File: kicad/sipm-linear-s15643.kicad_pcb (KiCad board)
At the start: 4 copper layers, 92.2 x 68.9 mm, 164 parts, among them J1 SSQ-103-01-G-D, J12 Conn_Coaxial, J13 Conn_Coaxial, J2 Conn_Coaxial, J3 Conn_Coaxial, J4 Conn_Coaxial, J5 Conn_Coaxial, J6 Conn_Coaxial, J7 Conn_Coaxial, J8 Conn_Coaxial, J9 Conn_Coaxial, U1 OPA847IDBVT, U12 OPA847IDBVT, U13 OPA847IDBVT, U2 S15643, U3 OPA847IDBVT, U4 OPA847IDBVT, U5 OPA847IDBVT, U6 OPA847IDBVT, U7 OPA847IDBVT, U8 OPA847IDBVT, U9 OPA847IDBVT

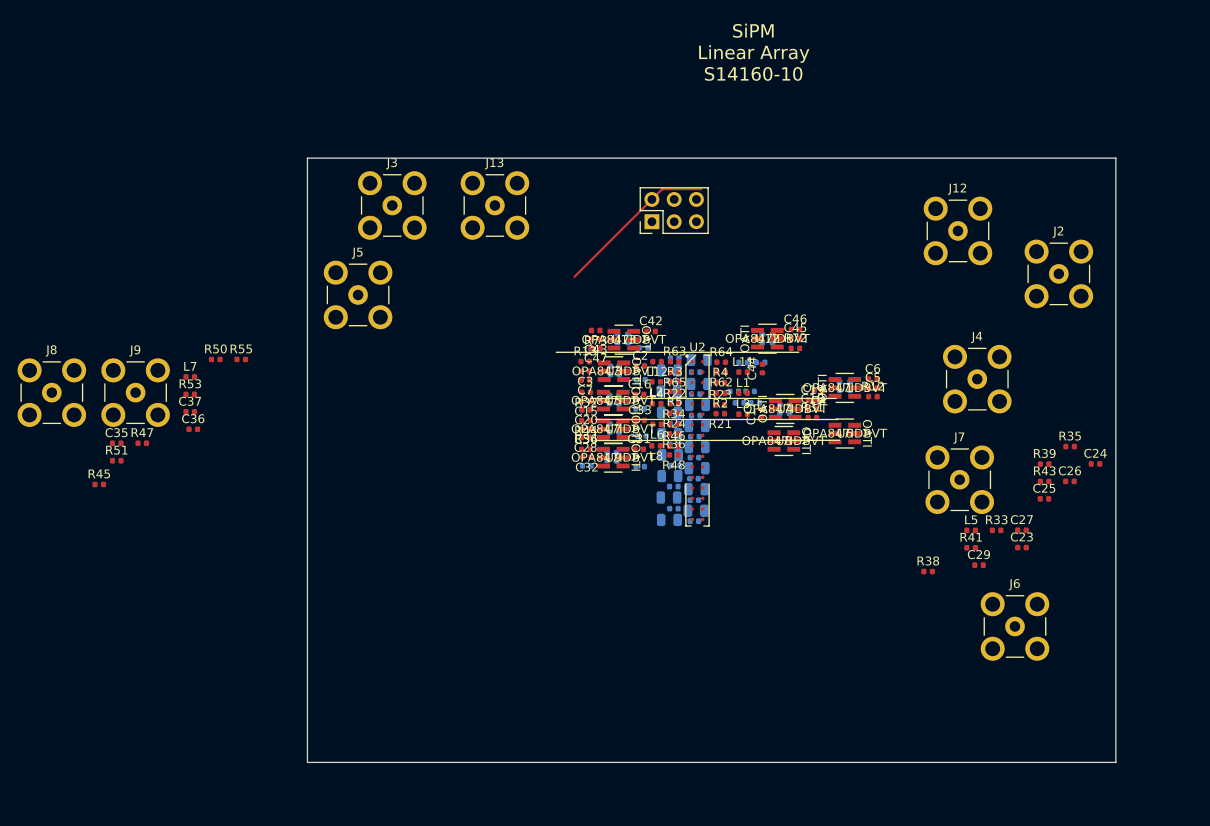
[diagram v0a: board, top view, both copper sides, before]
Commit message: Update layout for the new footprint
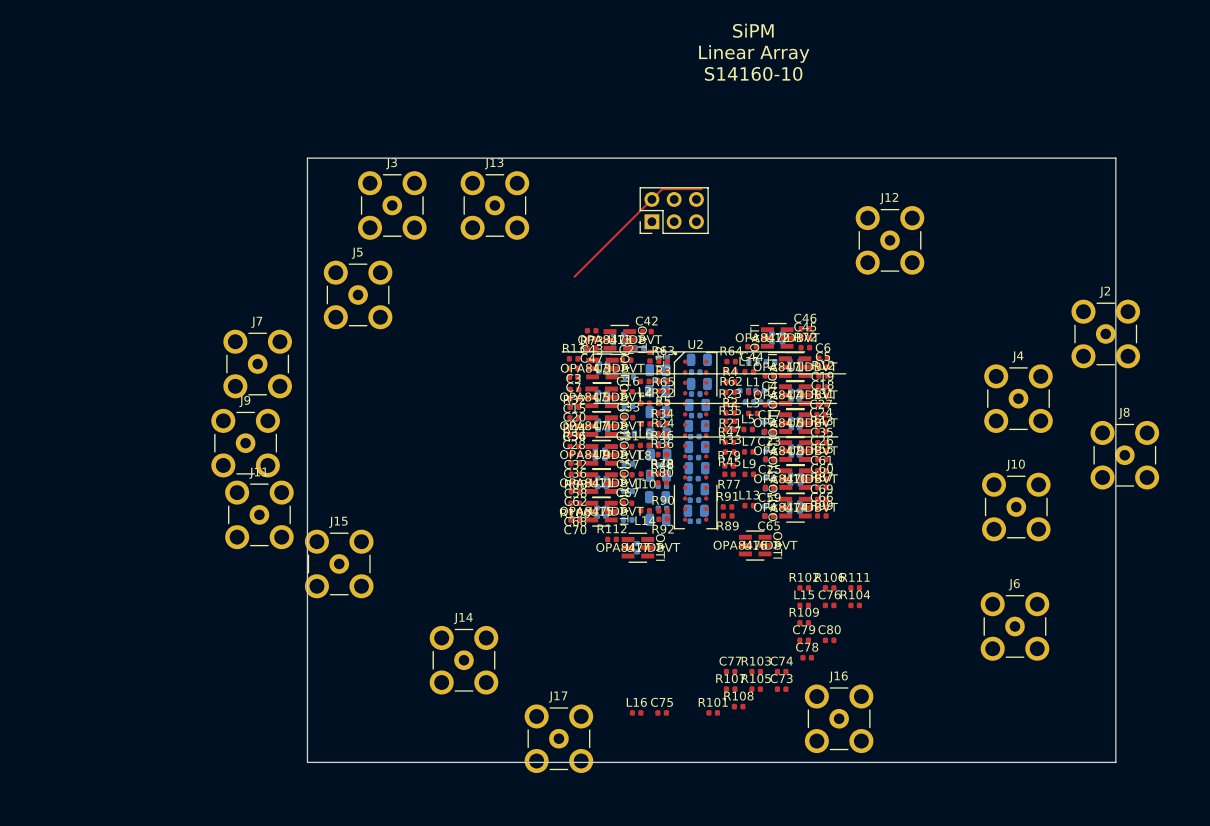
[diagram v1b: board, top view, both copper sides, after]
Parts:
- added C57: 1u, Capacitor_SMD:C_0402_1005Metric, F.Cu at (175.8, 105.3)
- added C58: 1u, Capacitor_SMD:C_0402_1005Metric, F.Cu at (169.9, 106.3)
- added C59: 1u, Capacitor_SMD:C_0402_1005Metric, F.Cu at (192.0, 106.8)
- added C60: 1u, Capacitor_SMD:C_0402_1005Metric, F.Cu at (198.0, 105.8)
- added C61: 1u, Capacitor_SMD:C_0402_1005Metric, F.Cu at (198.0, 104.8)
- added C62: 1u, Capacitor_SMD:C_0402_1005Metric, F.Cu at (169.9, 107.2)
- added C63: 1p, Capacitor_SMD:C_0402_1005Metric, B.Cu at (195.5, 105.9)
- added C64: 1p, Capacitor_SMD:C_0402_1005Metric, B.Cu at (173.4, 106.2)
- added C65: 1u, Capacitor_SMD:C_0402_1005Metric, F.Cu at (192.0, 110.0)
- added C66: 1u, Capacitor_SMD:C_0402_1005Metric, F.Cu at (198.0, 109.0)
- added C67: 1u, Capacitor_SMD:C_0402_1005Metric, F.Cu at (175.8, 108.5)
- added C68: 1u, Capacitor_SMD:C_0402_1005Metric, F.Cu at (169.9, 109.5)
- added C69: 1u, Capacitor_SMD:C_0402_1005Metric, F.Cu at (198.0, 108.1)
- added C70: 1u, Capacitor_SMD:C_0402_1005Metric, F.Cu at (169.9, 110.5)
- added C71: 1p, Capacitor_SMD:C_0402_1005Metric, B.Cu at (194.3, 109.0)
- added C72: 1p, Capacitor_SMD:C_0402_1005Metric, B.Cu at (173.4, 109.6)
- added C73: 1u, Capacitor_SMD:C_0402_1005Metric, F.Cu at (193.4, 129.8)
- added C74: 1u, Capacitor_SMD:C_0402_1005Metric, F.Cu at (193.4, 127.8)
- added C75: 1u, Capacitor_SMD:C_0402_1005Metric, F.Cu at (179.8, 132.5)
- added C76: 1u, Capacitor_SMD:C_0402_1005Metric, F.Cu at (198.9, 120.2)
- added C77: 1u, Capacitor_SMD:C_0402_1005Metric, F.Cu at (187.6, 127.8)
- added C78: 1u, Capacitor_SMD:C_0402_1005Metric, F.Cu at (196.3, 126.2)
- added C79: 1p, Capacitor_SMD:C_0402_1005Metric, F.Cu at (196.0, 124.2)
- added C80: 1p, Capacitor_SMD:C_0402_1005Metric, F.Cu at (198.9, 124.2)
- added J10: Conn_Coaxial, Connector_Coaxial:SMB_Jack_Vertical, F.Cu at (220.2, 109.0)
- added J11: Conn_Coaxial, Connector_Coaxial:SMB_Jack_Vertical, F.Cu at (133.8, 109.9)
- added J14: Conn_Coaxial, Connector_Coaxial:SMB_Jack_Vertical, F.Cu at (157.2, 126.5)
- added J15: Conn_Coaxial, Connector_Coaxial:SMB_Jack_Vertical, F.Cu at (142.9, 115.5)
- added J16: Conn_Coaxial, Connector_Coaxial:SMB_Jack_Vertical, F.Cu at (199.9, 133.1)
- added J17: Conn_Coaxial, Connector_Coaxial:SMB_Jack_Vertical, F.Cu at (168.0, 135.4)
- added L10: 0.033uH, footprints:C_0402_1005Metric, F.Cu at (177.9, 105.2)
- added L13: 0.033uH, footprints:C_0402_1005Metric, F.Cu at (189.7, 108.8)
- added L14: 0.033uH, footprints:C_0402_1005Metric, F.Cu at (177.8, 109.4)
- added L15: 0.033uH, footprints:C_0402_1005Metric, F.Cu at (196.0, 120.2)
- added L16: 0.033uH, footprints:C_0402_1005Metric, F.Cu at (176.9, 132.5)
- added L9: 0.033uH, footprints:C_0402_1005Metric, F.Cu at (189.7, 105.2)
- added R100: 50, footprints:R_0402_1005Metric, F.Cu at (169.8, 108.5)
- added R101: 3.3, footprints:R_0402_1005Metric, F.Cu at (185.6, 132.5)
- added R102: 3.3, footprints:R_0402_1005Metric, F.Cu at (196.0, 118.2)
- added R103: 33, footprints:R_0402_1005Metric, F.Cu at (190.5, 127.8)
- added R104: 33, footprints:R_0402_1005Metric, F.Cu at (201.8, 120.2)
- added R105: 5000, footprints:R_0402_1005Metric, F.Cu at (190.5, 129.8)
- added R106: 5000, footprints:R_0402_1005Metric, F.Cu at (198.9, 118.2)
- added R107: 5000, footprints:R_0402_1005Metric, F.Cu at (187.6, 129.8)
- added R108: 5000, footprints:R_0402_1005Metric, F.Cu at (188.5, 131.7)
- added R109: 1.5k, footprints:R_0402_1005Metric, F.Cu at (196.0, 122.2)
- added R110: 1.5k, footprints:R_0402_1005Metric, B.Cu at (176.9, 113.6)
- added R111: 50, footprints:R_0402_1005Metric, F.Cu at (201.8, 118.2)
- added R112: 50, footprints:R_0402_1005Metric, F.Cu at (174.1, 112.7)
- added R77: 3.3, footprints:R_0402_1005Metric, F.Cu at (187.4, 105.2)
- added R78: 3.3, footprints:R_0402_1005Metric, F.Cu at (179.8, 105.2)
- added R79: 33, footprints:R_0402_1005Metric, F.Cu at (187.4, 104.3)
- added R80: 33, footprints:R_0402_1005Metric, F.Cu at (179.8, 106.2)
- added R81: 5000, footprints:R_0402_1005Metric, B.Cu at (175.9, 107.2)
- added R82: 5000, footprints:R_0402_1005Metric, B.Cu at (192.0, 105.7)
- added R83: 5000, footprints:R_0402_1005Metric, B.Cu at (192.0, 106.9)
- added R84: 5000, footprints:R_0402_1005Metric, B.Cu at (169.9, 107.2)
- added R85: 1.5k, footprints:R_0402_1005Metric, B.Cu at (194.4, 105.8)
- added R86: 1.5k, footprints:R_0402_1005Metric, B.Cu at (172.4, 106.2)
- added R87: 50, footprints:R_0402_1005Metric, F.Cu at (198.0, 106.8)
- added R88: 50, footprints:R_0402_1005Metric, F.Cu at (169.9, 105.3)
- added R89: 3.3, footprints:R_0402_1005Metric, F.Cu at (187.2, 110.0)
- added R90: 3.3, footprints:R_0402_1005Metric, F.Cu at (179.9, 109.4)
- added R91: 33, footprints:R_0402_1005Metric, F.Cu at (187.2, 109.0)
- added R92: 33, footprints:R_0402_1005Metric, F.Cu at (179.9, 110.4)
- added R93: 5000, footprints:R_0402_1005Metric, B.Cu at (175.8, 110.5)
- added R94: 5000, footprints:R_0402_1005Metric, B.Cu at (192.0, 110.0)
- added R95: 5000, footprints:R_0402_1005Metric, B.Cu at (192.0, 109.0)
- added R96: 5000, footprints:R_0402_1005Metric, B.Cu at (169.9, 110.5)
- added R97: 1.5k, footprints:R_0402_1005Metric, B.Cu at (195.5, 109.0)
- added R98: 1.5k, footprints:R_0402_1005Metric, B.Cu at (172.3, 109.6)
- added R99: 50, footprints:R_0402_1005Metric, F.Cu at (198.0, 110.0)
- added U10: OPA847IDBVT, footprints:OPA847IDBVT, F.Cu at (195.0, 105.8)
- added U11: OPA847IDBVT, footprints:OPA847IDBVT, F.Cu at (172.9, 106.3)
- added U14: OPA847IDBVT, footprints:OPA847IDBVT, F.Cu at (195.0, 109.0)
- added U15: OPA847IDBVT, footprints:OPA847IDBVT, F.Cu at (172.8, 109.5)
- added U16: OPA847IDBVT, footprints:OPA847IDBVT, F.Cu at (190.4, 113.4)
- added U17: OPA847IDBVT, footprints:OPA847IDBVT, F.Cu at (177.0, 113.6)
- C29, C37, R38, R39, R41, R50, R51, R53: moved to B.Cu
- U2: footprint footprints:S15643-N16 -> S13615-1025:AF210729-S14160-x16
- moved J8 122.6 mm to (232.5, 103.1)
- moved J7 81.1 mm to (133.7, 92.7)
- moved C35 80.4 mm to (198.0, 101.7)
- moved R51 74.5 mm to (192.0, 103.5)
- moved R45 72.0 mm to (187.5, 102.7), turned to 180 degrees
- moved C37 69.6 mm to (195.4, 102.6), turned to -90 degrees
- moved R53 68.8 mm to (194.5, 102.6), turned to -90 degrees
- moved R55 67.2 mm to (198.0, 103.5)
- moved R47 67.0 mm to (187.4, 101.6)
- moved L7 64.3 mm to (189.7, 102.7)
- moved R50 64.0 mm to (192.1, 102.6), turned to 180 degrees
- moved C36 43.7 mm to (169.8, 104.0), turned to 180 degrees
- moved R35 38.9 mm to (187.5, 99.2)
- moved R33 32.5 mm to (187.5, 100.2), turned to 180 degrees
- moved C23 31.7 mm to (192.0, 100.4), turned to 180 degrees
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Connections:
- C50 pad 1: Net-(U2-Pad19) -> Net-(C50-Pad1)
- C51 pad 1: Net-(U2-Pad21) -> Net-(C51-Pad1)
- C52 pad 1: Net-(U2-Pad23) -> Net-(C52-Pad1)
- C53 pad 1: Net-(U2-Pad25) -> Net-(C53-Pad1)
- C54 pad 1: Net-(U2-Pad27) -> Net-(C54-Pad1)
- C55 pad 1: Net-(U2-Pad29) -> Net-(C55-Pad1)
- C56 pad 1: Net-(U2-Pad31) -> Net-(C56-Pad1)
- R60 pad 2: Net-(U2-Pad19) -> Net-(C50-Pad1)
- R61 pad 2: Net-(U2-Pad21) -> Net-(C51-Pad1)
- R66 pad 2: Net-(U2-Pad23) -> Net-(C52-Pad1)
- R67 pad 2: Net-(U2-Pad25) -> Net-(C53-Pad1)
- R74 pad 2: Net-(U2-Pad27) -> Net-(C54-Pad1)
- R75 pad 2: Net-(U2-Pad29) -> Net-(C55-Pad1)
- R76 pad 2: Net-(U2-Pad31) -> Net-(C56-Pad1)

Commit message: Update layout and fix array footprint
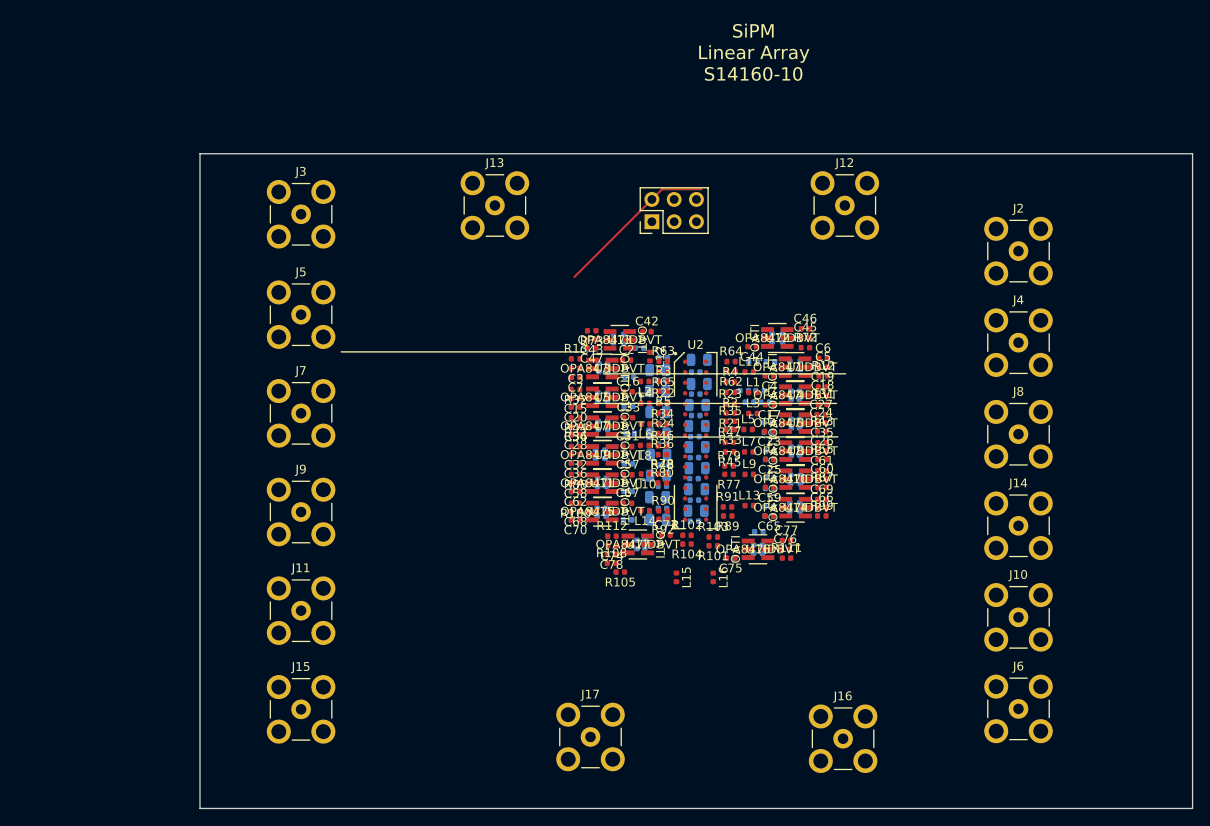
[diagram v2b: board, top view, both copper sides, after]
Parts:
- C79, C80, R106, R107, R109: moved to B.Cu
- J10, J11, J12, J13, J14, J15, J16, J17, J2, J3, J4, J5, J6, J7, J8, J9: footprint Connector_Coaxial:SMB_Jack_Vertical -> footprints:SMB_Jack_Vertical
- moved J14 65.1 mm to (220.4, 111.1)
- moved C78 25.2 mm to (174.0, 114.4), turned to 180 degrees
- moved C74 24.1 mm to (174.1, 113.4), turned to 180 degrees
- moved C80 23.8 mm to (177.8, 113.2), turned to -90 degrees
- moved C73 22.0 mm to (180.2, 112.2)
- moved R108 21.8 mm to (174.0, 115.4)
- moved R105 20.4 mm to (175.0, 116.4), turned to 180 degrees
- moved R104 20.4 mm to (182.6, 113.2), turned to 180 degrees
- moved C75 19.3 mm to (187.6, 114.8), turned to 180 degrees
- moved R101 19.1 mm to (185.6, 113.4), turned to 180 degrees
- moved R107 18.2 mm to (190.8, 111.8), turned to 180 degrees
- moved L16 17.8 mm to (185.6, 117.0), turned to -90 degrees
- moved J15 17.1 mm to (138.6, 132.1)
- moved C77 16.3 mm to (193.9, 112.8)
- moved R103 16.1 mm to (185.6, 112.4)
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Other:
- board size 92.2 x 68.9 mm -> 113.2 x 74.6 mm

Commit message: Update foot print for the revised hamamatsu part
They only have 2 cathode connections.  In addition, add a second power connector, since at least two power supplies are going to be needed.
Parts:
- removed C13, C50, C51, C52, C53, C54, C55, C56: 1u, Capacitor_SMD:C_0805_2012Metric
- removed R16, R17, R18, R19, R20, R57, R58, R60, R61, R66, R67, R74, R75, R76: 10, footprints:R_0402_1005Metric
- moved C12 8.93 mm to (184.0, 88.2), turned to 0 degrees
- moved C10 5.67 mm to (184.0, 90.2), turned to 0 degrees
- moved C11 0.75 mm to (184.0, 94.2), turned to 0 degrees
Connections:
- C1 pad 1: Net-(C1-Pad1) -> Net-(C11-Pad1)
- C10 pad 1: Net-(C10-Pad1) -> Net-(C11-Pad1)
- C12 pad 1: Net-(C12-Pad1) -> Net-(C11-Pad1)
- C39 pad 1: Net-(C39-Pad1) -> Net-(C14-Pad1)
- C40 pad 1: Net-(C40-Pad1) -> Net-(C14-Pad1)
- C41 pad 1: Net-(C41-Pad1) -> Net-(C14-Pad1)
- R1 pad 2: Net-(C1-Pad1) -> Net-(C11-Pad1)
- R59 pad 1: Net-(R16-Pad1) -> (no net)
- R59 pad 2: Net-(C41-Pad1) -> Net-(C14-Pad1)
- U2 pad 1: Net-(C1-Pad1) -> Net-(C11-Pad1)
- U2 pad 11: Net-(C14-Pad1) -> (no net)
- U2 pad 13: Net-(C39-Pad1) -> (no net)
- U2 pad 15: Net-(C40-Pad1) -> (no net)
- U2 pad 17: Net-(C41-Pad1) -> Net-(C14-Pad1)
- U2 pad 19: Net-(C50-Pad1) -> (no net)
- U2 pad 21: Net-(C51-Pad1) -> (no net)
- U2 pad 23: Net-(C52-Pad1) -> (no net)
- U2 pad 25: Net-(C53-Pad1) -> (no net)
- U2 pad 27: Net-(C54-Pad1) -> (no net)
- U2 pad 29: Net-(C55-Pad1) -> (no net)
- U2 pad 3: Net-(C10-Pad1) -> (no net)
- U2 pad 31: Net-(C56-Pad1) -> (no net)
- U2 pad 5: Net-(C11-Pad1) -> (no net)
- U2 pad 7: Net-(C12-Pad1) -> (no net)
- U2 pad 9: Net-(C13-Pad1) -> (no net)
